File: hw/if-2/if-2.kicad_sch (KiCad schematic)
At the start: 4 parts

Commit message: Docs
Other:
- note added: "Software Defined Repeater Controller - Radio Interface Board"
- note removed: "Digital Repeater Controller V2 - Radio Interface Board"
- title: Digital Repeater Controller -> Software Defined Repeater Controller
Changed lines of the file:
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@@
 	(paper "USLetter")
 	(title_block
-		(title "Digital Repeater Controller")
-		(date "2025-05-31")
-		(rev "2")
+		(title "Software Defined Repeater Controller")
+		(date "2025-06-21")
+		(rev "3")
 		(company "Bruce MacKinnon KC1FSZ")
 		(comment 1 "Copyright (C) Bruce MacKinnon, 2025")
@@
 		)
 	)
-	(text "Digital Repeater Controller V2 - Radio Interface Board"
+	(text "Software Defined Repeater Controller - Radio Interface Board"
 		(exclude_from_sim no)
 		(at 71.374 21.082 0)

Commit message: Updated audio file to 16K
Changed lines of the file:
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@@
 	(text "Software Defined Repeater Controller - Radio Interface Board"
 		(exclude_from_sim no)
-		(at 71.374 21.082 0)
+		(at 77.978 20.828 0)
 		(effects
 			(font

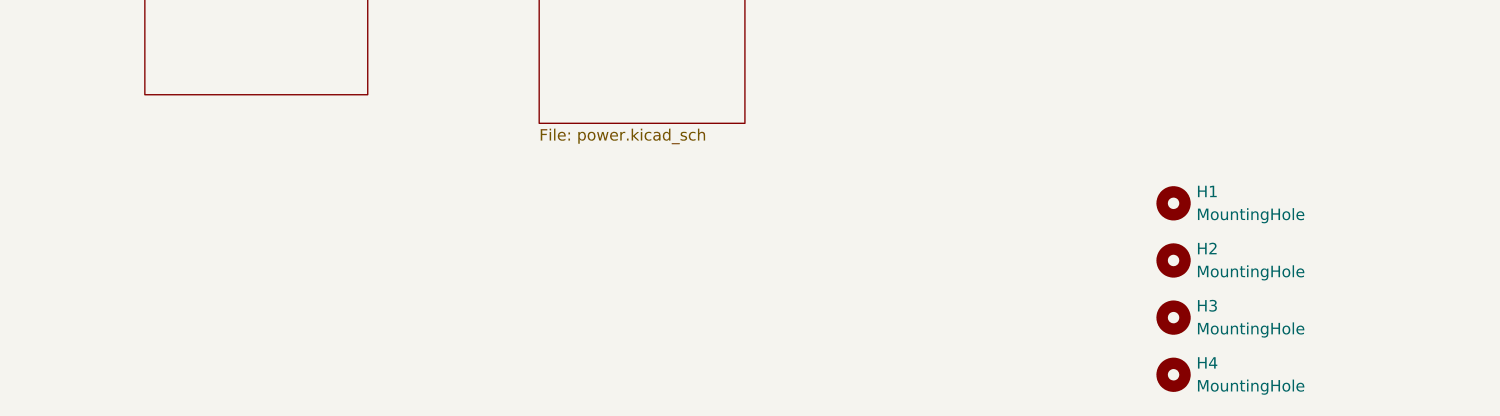
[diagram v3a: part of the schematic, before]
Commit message: Updating schematics, create new mini-board for radio interface
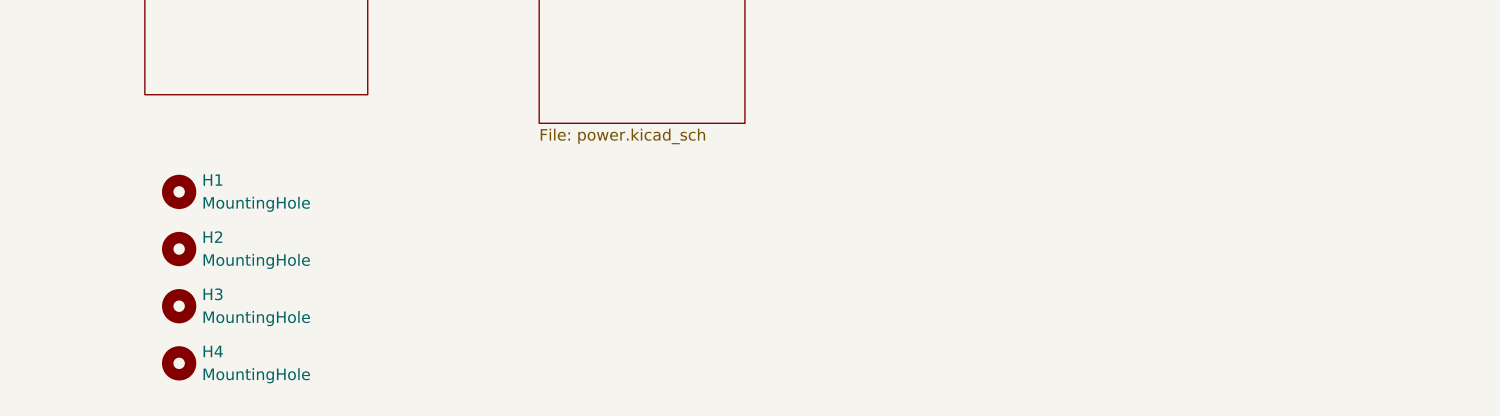
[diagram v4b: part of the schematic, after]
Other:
- moved on the sheet: H1, H2, H3, H4
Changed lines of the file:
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@@
 	(symbol
 		(lib_id "Mechanical:MountingHole")
-		(at 133.35 186.69 0)
+		(at 22.86 185.42 0)
 		(unit 1)
 		(exclude_from_sim yes)
@@
 		(fields_autoplaced yes)
 		(property "Reference" "H3"
-			(at 135.89 185.4199 0)
-			(effects
-				(font
-					(size 1.27 1.27)
-				)
-				(justify left)
-			)
-		)
-		(property "Value" "MountingHole"
-			(at 135.89 187.9599 0)
-			(effects
-				(font
-					(size 1.27 1.27)
-				)
-				(justify left)
-			)
-		)
-		(property "Footprint" "MountingHole:MountingHole_3.5mm"
-			(at 133.35 186.69 0)
-			(effects
-				(font
-					(size 1.27 1.27)
-				)
-				(hide yes)
-			)
-		)
-		(property "Datasheet" "~"
-			(at 133.35 186.69 0)
-			(effects
-				(font
-					(size 1.27 1.27)
-				)
-				(hide yes)
-			)
-		)
-		(property "Description" "Mounting Hole without connection"
-			(at 133.35 186.69 0)
+			(at 25.4 184.1499 0)
+			(effects
+				(font
+					(size 1.27 1.27)
+				)
+				(justify left)
+			)
+		)
+		(property "Value" "MountingHole"
+			(at 25.4 186.6899 0)
+			(effects
+				(font
+					(size 1.27 1.27)
+				)
+				(justify left)
+			)
+		)
+		(property "Footprint" "MountingHole:MountingHole_3.5mm"
+			(at 22.86 185.42 0)
+			(effects
+				(font
+					(size 1.27 1.27)
+				)
+				(hide yes)
+			)
+		)
+		(property "Datasheet" "~"
+			(at 22.86 185.42 0)
+			(effects
+				(font
+					(size 1.27 1.27)
+				)
+				(hide yes)
+			)
+		)
+		(property "Description" "Mounting Hole without connection"
+			(at 22.86 185.42 0)
 			(effects
 				(font
@@
 	(symbol
 		(lib_id "Mechanical:MountingHole")
-		(at 133.35 180.34 0)
+		(at 22.86 179.07 0)
 		(unit 1)
 		(exclude_from_sim yes)
@@
 		(fields_autoplaced yes)
 		(property "Reference" "H2"
-			(at 135.89 179.0699 0)
-			(effects
-				(font
-					(size 1.27 1.27)
-				)
-				(justify left)
-			)
-		)
-		(property "Value" "MountingHole"
-			(at 135.89 181.6099 0)
-			(effects
-				(font
-					(size 1.27 1.27)
-				)
-				(justify left)
-			)
-		)
-		(property "Footprint" "MountingHole:MountingHole_3.5mm"
-			(at 133.35 180.34 0)
-			(effects
-				(font
-					(size 1.27 1.27)
-				)
-				(hide yes)
-			)
-		)
-		(property "Datasheet" "~"
-			(at 133.35 180.34 0)
-			(effects
-				(font
-					(size 1.27 1.27)
-				)
-				(hide yes)
-			)
-		)
-		(property "Description" "Mounting Hole without connection"
-			(at 133.35 180.34 0)
+			(at 25.4 177.7999 0)
+			(effects
+				(font
+					(size 1.27 1.27)
+				)
+				(justify left)
+			)
+		)
+		(property "Value" "MountingHole"
+			(at 25.4 180.3399 0)
+			(effects
+				(font
+					(size 1.27 1.27)
+				)
+				(justify left)
+			)
+		)
+		(property "Footprint" "MountingHole:MountingHole_3.5mm"
+			(at 22.86 179.07 0)
+			(effects
+				(font
+					(size 1.27 1.27)
+				)
+				(hide yes)
+			)
+		)
+		(property "Datasheet" "~"
+			(at 22.86 179.07 0)
+			(effects
+				(font
+					(size 1.27 1.27)
+				)
+				(hide yes)
+			)
+		)
+		(property "Description" "Mounting Hole without connection"
+			(at 22.86 179.07 0)
 			(effects
 				(font
@@
 	(symbol
 		(lib_id "Mechanical:MountingHole")
-		(at 133.35 193.04 0)
+		(at 22.86 191.77 0)
 		(unit 1)
 		(exclude_from_sim yes)
@@
 		(fields_autoplaced yes)
 		(property "Reference" "H4"
-			(at 135.89 191.7699 0)
-			(effects
-				(font
-					(size 1.27 1.27)
-				)
-				(justify left)
-			)
-		)
-		(property "Value" "MountingHole"
-			(at 135.89 194.3099 0)
-			(effects
-				(font
-					(size 1.27 1.27)
-				)
-				(justify left)
-			)
-		)
-		(property "Footprint" "MountingHole:MountingHole_3.5mm"
-			(at 133.35 193.04 0)
-			(effects
-				(font
-					(size 1.27 1.27)
-				)
-				(hide yes)
-			)
-		)
-		(property "Datasheet" "~"
-			(at 133.35 193.04 0)
-			(effects
-				(font
-					(size 1.27 1.27)
-				)
-				(hide yes)
-			)
-		)
-		(property "Description" "Mounting Hole without connection"
-			(at 133.35 193.04 0)
+			(at 25.4 190.4999 0)
+			(effects
+				(font
+					(size 1.27 1.27)
+				)
+				(justify left)
+			)
+		)
+		(property "Value" "MountingHole"
+			(at 25.4 193.0399 0)
+			(effects
+				(font
+					(size 1.27 1.27)
+				)
+				(justify left)
+			)
+		)
+		(property "Footprint" "MountingHole:MountingHole_3.5mm"
+			(at 22.86 191.77 0)
+			(effects
+				(font
+					(size 1.27 1.27)
+				)
+				(hide yes)
+			)
+		)
+		(property "Datasheet" "~"
+			(at 22.86 191.77 0)
+			(effects
+				(font
+					(size 1.27 1.27)
+				)
+				(hide yes)
+			)
+		)
+		(property "Description" "Mounting Hole without connection"
+			(at 22.86 191.77 0)
 			(effects
 				(font
@@
 	(symbol
 		(lib_id "Mechanical:MountingHole")
-		(at 133.35 173.99 0)
+		(at 22.86 172.72 0)
 		(unit 1)
 		(exclude_from_sim yes)
@@
 		(fields_autoplaced yes)
 		(property "Reference" "H1"
-			(at 135.89 172.7199 0)
-			(effects
-				(font
-					(size 1.27 1.27)
-				)
-				(justify left)
-			)
-		)
-		(property "Value" "MountingHole"
-			(at 135.89 175.2599 0)
-			(effects
-				(font
-					(size 1.27 1.27)
-				)
-				(justify left)
-			)
-		)
-		(property "Footprint" "MountingHole:MountingHole_3.5mm"
-			(at 133.35 173.99 0)
-			(effects
-				(font
-					(size 1.27 1.27)
-				)
-				(hide yes)
-			)
-		)
-		(property "Datasheet" "~"
-			(at 133.35 173.99 0)
-			(effects
-				(font
-					(size 1.27 1.27)
-				)
-				(hide yes)
-			)
-		)
-		(property "Description" "Mounting Hole without connection"
-			(at 133.35 173.99 0)
-			(effects
-				(font
+			(at 25.4 171.4499 0)
+			(effects
+				(font
+					(size 1.27 1.27)
+				)
+				(justify left)
+			)
+		)
+		(property "Value" "MountingHole"
+			(at 25.4 173.9899 0)
+			(effects
+				(font
+					(size 1.27 1.27)
+				)
+				(justify left)
+			)
+		)
+		(property "Footprint" "MountingHole:MountingHole_3.5mm"
+			(at 22.86 172.72 0)
+			(effects
+				(font
+					(size 1.27 1.27)
+				)
+				(hide yes)
+			)
+		)
+		(property "Datasheet" "~"
+			(at 22.86 172.72 0)
+			(effects
+				(font
+					(size 1.27 1.27)
+				)
+				(hide yes)
+			)
+		)
+		(property "Description" "Mounting Hole without connection"
+			(at 22.86 172.72 0)
+			(effects
+				(font
